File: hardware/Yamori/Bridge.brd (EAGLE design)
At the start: 50.5 x 55.9 mm, 14 parts, among them J1 CONN_20X2, U3 SN74LS244N

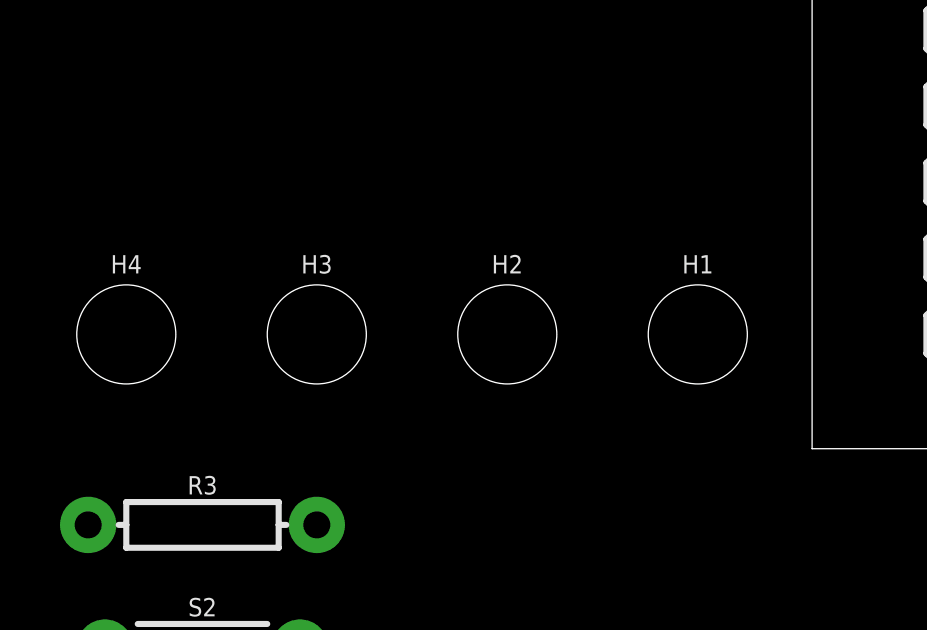
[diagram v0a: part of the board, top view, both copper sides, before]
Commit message: Holes removed
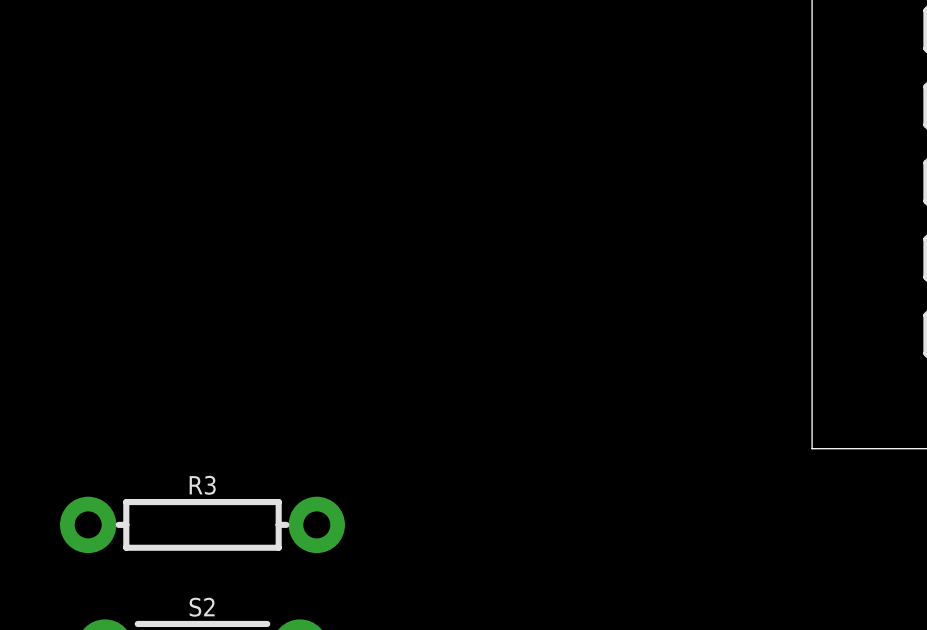
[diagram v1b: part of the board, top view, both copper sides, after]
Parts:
- removed H1, H2, H3, H4: STAND-OFF, SparkFun-Hardware:STAND-OFF
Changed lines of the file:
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@@
 <attribute name="VALUE" x="49.9618" y="21.971" size="2.0828" layer="27" ratio="10" rot="SR0"/>
-</element>
-<element name="H1" library="SparkFun-Hardware" package="STAND-OFF" value="STAND-OFF" x="21.59" y="13.97" smashed="yes">
-<attribute name="NAME" x="21.59" y="16.002" size="0.6096" layer="25" font="vector" ratio="20" align="bottom-center"/>
-<attribute name="VALUE" x="21.59" y="11.938" size="0.6096" layer="27" font="vector" ratio="20" align="top-center"/>
-</element>
-<element name="H2" library="SparkFun-Hardware" package="STAND-OFF" value="STAND-OFF" x="15.24" y="13.97" smashed="yes">
-<attribute name="NAME" x="15.24" y="16.002" size="0.6096" layer="25" font="vector" ratio="20" align="bottom-center"/>
-<attribute name="VALUE" x="15.24" y="11.938" size="0.6096" layer="27" font="vector" ratio="20" align="top-center"/>
-</element>
-<element name="H3" library="SparkFun-Hardware" package="STAND-OFF" value="STAND-OFF" x="8.89" y="13.97" smashed="yes">
-<attribute name="NAME" x="8.89" y="16.002" size="0.6096" layer="25" font="vector" ratio="20" align="bottom-center"/>
-<attribute name="VALUE" x="8.89" y="11.938" size="0.6096" layer="27" font="vector" ratio="20" align="top-center"/>
-</element>
-<element name="H4" library="SparkFun-Hardware" package="STAND-OFF" value="STAND-OFF" x="2.54" y="13.97" smashed="yes">
-<attribute name="NAME" x="2.54" y="16.002" size="0.6096" layer="25" font="vector" ratio="20" align="bottom-center"/>
-<attribute name="VALUE" x="2.54" y="11.938" size="0.6096" layer="27" font="vector" ratio="20" align="top-center"/>
 </element>
 <element name="S1" library="SparkFun-Switches" package="TACTILE_SWITCH_PTH_6.0MM" value="MOMENTARY-SWITCH-SPST-PTH-6.0MM" x="43.18" y="49.53" smashed="yes">

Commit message: Schema final version
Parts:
- R3: value (none) -> 4.7K
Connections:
- net BTN1 renamed !BTN1
- net PWR_OFF renamed !PWR_OFF
- removed net BCM13: J4.5
- net BCM3: now also J4.5
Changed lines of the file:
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@@
 <attribute name="VALUE" x="66.04" y="20.193" size="0.6096" layer="27" font="vector" ratio="20" rot="R180"/>
 </element>
-<element name="R3" library="SparkFun-Resistors" package="AXIAL-0.3" value=" " x="5.08" y="7.62" smashed="yes">
+<element name="R3" library="SparkFun-Resistors" package="AXIAL-0.3" value="4.7K" x="5.08" y="7.62" smashed="yes">
 <attribute name="NAME" x="5.08" y="8.636" size="0.6096" layer="25" font="vector" ratio="20" align="bottom-center"/>
 <attribute name="PROD_ID" value=" " x="5.08" y="7.62" size="1.778" layer="27" display="off"/>
@@
 <signal name="BCM3">
 <contactref element="J1" pad="5"/>
+<contactref element="J4" pad="5"/>
+<wire x1="59.69" y1="17.78" x2="30.48" y2="57.15" width="0" layer="19" extent="1-1"/>
 </signal>
 <signal name="BCM14">
@@
 <wire x1="62.23" y1="17.78" x2="33.02" y2="49.53" width="0" layer="19" extent="1-1"/>
 </signal>
-<signal name="BTN1">
+<signal name="!BTN1">
 <contactref element="J1" pad="11"/>
 <contactref element="S1" pad="3"/>
@@
 <wire x1="39.37" y1="41.91" x2="39.9288" y2="47.2694" width="0" layer="19" extent="1-1"/>
 <wire x1="30.48" y1="49.53" x2="39.9288" y2="47.2694" width="0" layer="19" extent="1-1"/>
-</signal>
-<signal name="PWR_OFF">
-<contactref element="J1" pad="13"/>
-<contactref element="R3" pad="P$1"/>
-<contactref element="S2" pad="3"/>
-<wire x1="1.27" y1="7.62" x2="30.48" y2="46.99" width="0" layer="19" extent="1-1"/>
-<wire x1="1.8288" y1="-0.9906" x2="1.27" y2="7.62" width="0" layer="19" extent="1-1"/>
 </signal>
 <signal name="BCM22">
@@
 <wire x1="33.02" y1="29.21" x2="54.61" y2="15.24" width="0" layer="19" extent="1-1"/>
 </signal>
-<signal name="BCM13">
-<contactref element="J4" pad="5"/>
+<signal name="!PWR_OFF">
+<contactref element="R3" pad="P$1"/>
+<contactref element="S2" pad="3"/>
+<contactref element="J1" pad="13"/>
+<wire x1="1.27" y1="7.62" x2="30.48" y2="46.99" width="0" layer="19" extent="1-1"/>
+<wire x1="1.8288" y1="-0.9906" x2="1.27" y2="7.62" width="0" layer="19" extent="1-1"/>
 </signal>
 </signals>

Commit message: Wiring in progress
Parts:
- added H1, H2: STAND-OFF, SparkFun-Hardware:STAND-OFF
- moved R1 36.2 mm to (13.3, 55.2)
- moved J2 33.0 mm to (14.0, 62.2)
- moved J4 29.4 mm to (37.5, 6.99)
- moved R3 29.1 mm to (15.2, 34.9), turned to 180 degrees
- moved J1 28.5 mm to (2.54, 56.5)
- moved S1 28.2 mm to (15.2, 45.7), turned to 90 degrees
- moved R2 28.1 mm to (15.2, 38.7), turned to 180 degrees
- moved S2 27.9 mm to (15.2, 27.3), turned to 270 degrees
- moved J3 27.9 mm to (41.9, 55.9)
- moved U3 27.3 mm to (32.4, 27.9)
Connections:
- net BCM22: now also J4.18
- net BCM24: no longer J4.18
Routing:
- net 1A3: track 0.00 -> 127.4 mm
- net 3.3V: track 0.00 -> 121.3 mm
- net 1A1: track 0.00 -> 108.5 mm
- net 5V: track 0.00 -> 105.9 mm, vias 0 -> 1
- net BCM18: track 0.00 -> 105.6 mm
- net 1A4: track 0.00 -> 99.0 mm
- net BCM3: track 0.00 -> 97.5 mm, vias 0 -> 1
- net 2A3: track 0.00 -> 97.3 mm, vias 0 -> 1
- net 2A1: track 0.00 -> 97.1 mm
- net 2A4: track 0.00 -> 95.2 mm, vias 0 -> 1
- net 2A2: track 0.00 -> 93.6 mm
- net 1A2: track 0.00 -> 89.5 mm
- net BCM15: track 0.00 -> 86.1 mm, vias 0 -> 2
- net BCM14: track 0.00 -> 85.8 mm, vias 0 -> 2
- net 2Y2: track 0.00 -> 66.9 mm
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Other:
- board size 50.5 x 55.9 mm -> 47.9 x 64.8 mm
